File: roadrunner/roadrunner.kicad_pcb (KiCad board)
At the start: 2 copper layers, 216.9 x 86.9 mm, 52 parts, among them J1 Battery_conn, J2 battery_conn_r, SW1 SW_Push, SW10 SW_Push, SW10_r1 SW_Push, SW11 SW_Push, SW11_r1 SW_Push, SW12 SW_Push, SW12_r1 SW_Push, SW13 SW_Push, SW13_r1 SW_Push, SW14 SW_Push, SW14_r1 SW_Push, SW15 SW_Push, SW15_r1 SW_Push, SW16 SW_Push, SW16_r1 SW_Push, SW17 SW_Push, SW17_r1 SW_Push, SW1_r1 SW_Push, SW2 SW_Push, SW2_r1 SW_Push, SW3 SW_Push, SW3_r1 SW_Push, SW4 SW_Push, SW4_r1 SW_Push, SW5 SW_Push, SW5_r1 SW_Push, SW6 SW_Push, SW6_r1 SW_Push, SW7 SW_Push, SW7_r1 SW_Push, SW8 SW_Push, SW8_r1 SW_Push, SW9 SW_Push, SW9_r1 SW_Push, U1 ProMicro-kbd, U2 ProMicro-kbd

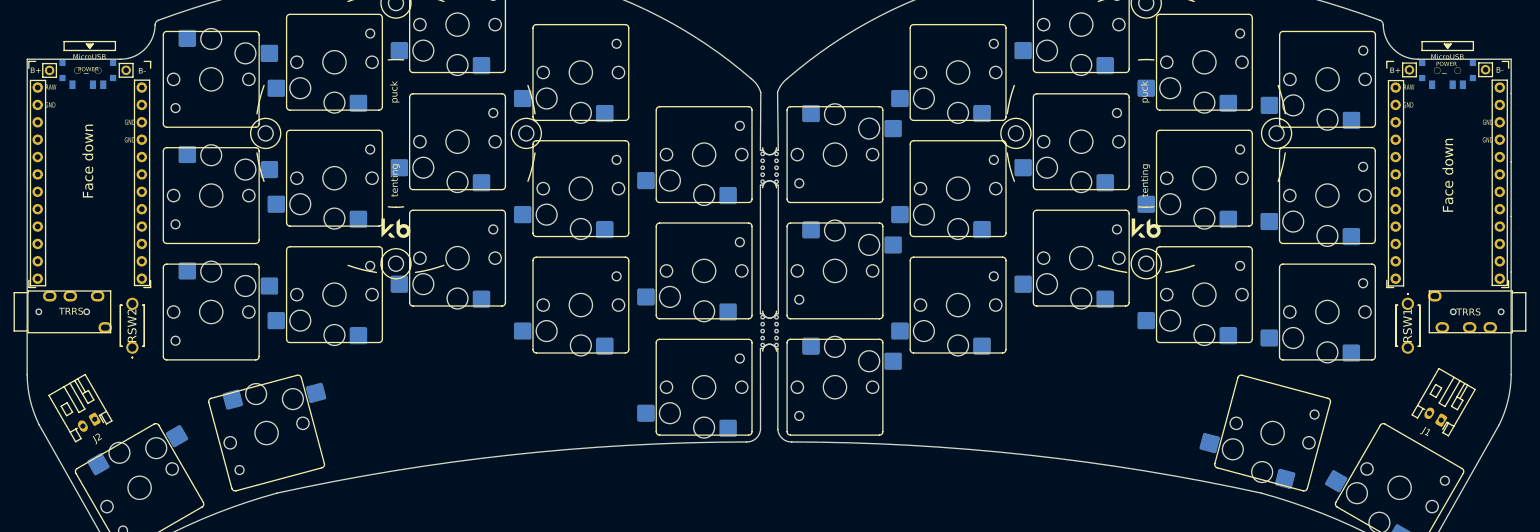
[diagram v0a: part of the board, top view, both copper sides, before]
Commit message: update schematic
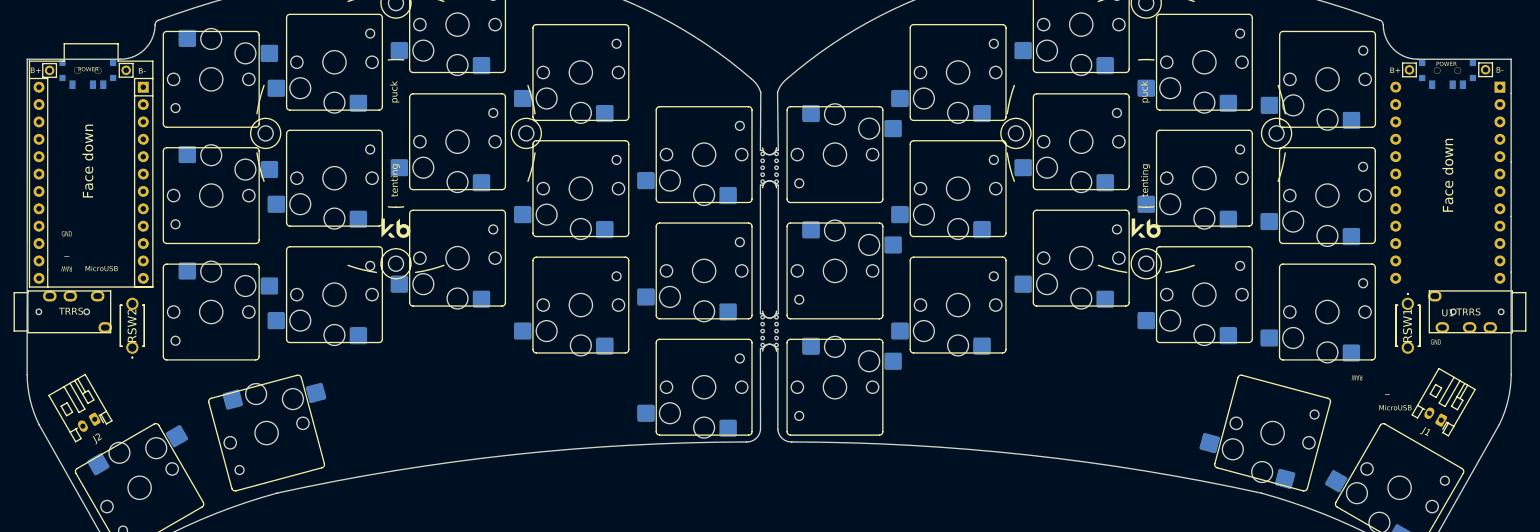
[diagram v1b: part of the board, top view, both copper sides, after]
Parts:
- U1, U2: footprint promicro:ProMicro_v3_min -> Arduino:Sparkfun_Pro_Micro; moved to B.Cu
- moved U2 16.8 mm to (43.8, 79.6)
- moved U1 15.4 mm to (243.1, 78.4)
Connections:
- U1 pad 1: (no net) -> Switch10
- U1 pad 10: (no net) -> Switch1
- U1 pad 11: (no net) -> Switch16
- U1 pad 12: (no net) -> Switch17
- U1 pad 13: (no net) -> Switch9
- U1 pad 14: (no net) -> Switch8
- U1 pad 15: (no net) -> Switch7
- U1 pad 16: (no net) -> Switch6
- U1 pad 17: (no net) -> Switch2
- U1 pad 18: (no net) -> Switch3
- U1 pad 19: (no net) -> Switch4
- U1 pad 2: (no net) -> Switch18
- U1 pad 20: (no net) -> Switch5
- U1 pad 21: (no net) -> vcc
- U1 pad 22: (no net) -> reset
- U1 pad 23: (no net) -> gnd
- U1 pad 24: (no net) -> raw
- U1 pad 3: (no net) -> gnd
- U1 pad 4: (no net) -> gnd
- U1 pad 5: (no net) -> Switch11
- U1 pad 6: (no net) -> Switch12
- U1 pad 7: (no net) -> Switch13
- U1 pad 8: (no net) -> Switch14
- U1 pad 9: (no net) -> Switch15
- U2 pad 1: (no net) -> Switch10_r
- U2 pad 10: (no net) -> Switch1_r
- U2 pad 11: (no net) -> Switch16_r
- U2 pad 12: (no net) -> Switch17_r
- U2 pad 13: (no net) -> Switch9_r
- U2 pad 14: (no net) -> Switch8_r
- U2 pad 15: (no net) -> Switch7_r
- U2 pad 16: (no net) -> Switch6_r
- U2 pad 17: (no net) -> Switch2_r
- U2 pad 18: (no net) -> Switch3_r
- U2 pad 19: (no net) -> Switch4_r
- U2 pad 2: (no net) -> Switch18_r
- U2 pad 20: (no net) -> Switch5_r
- U2 pad 21: (no net) -> vcc_r
- U2 pad 22: (no net) -> reset_r
- U2 pad 23: (no net) -> gnd_r
- U2 pad 24: (no net) -> raw_r
- U2 pad 3: (no net) -> gnd_r
- U2 pad 4: (no net) -> gnd_r
- U2 pad 5: (no net) -> Switch11_r
- U2 pad 6: (no net) -> Switch12_r
- U2 pad 7: (no net) -> Switch13_r
- U2 pad 8: (no net) -> Switch14_r
- U2 pad 9: (no net) -> Switch15_r

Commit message: update shape
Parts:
- TRRS1, TRRS2: footprint trrs:TRRS-PJ-320A -> Connector_Audio:Jack_3.5mm_PJ320E_Horizontal
- moved TRRS2 10.6 mm to (52.6, 88.2)
- moved TRRS1 9.47 mm to (250.7, 82.1)
- moved J2 1.77 mm to (54.3, 98.0)
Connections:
- TRRS1 pad R1: (no net) -> Switch18
- TRRS1 pad R2: (no net) -> vcc
- TRRS1 pad S: (no net) -> gnd
- TRRS1 pad T: (no net) -> gnd
- TRRS2 pad R1: (no net) -> Switch18_r
- TRRS2 pad R2: (no net) -> vcc_r
- TRRS2 pad S: (no net) -> gnd_r
- TRRS2 pad T: (no net) -> gnd_r
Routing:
- net gnd: track 0.00 -> 338.8 mm
- net gnd_r: track 0.00 -> 334.2 mm
- net Switch11_r: track 0.00 -> 108.4 mm
- net Switch6_r: track 0.00 -> 107.4 mm, vias 0 -> 1
- net Switch11: track 0.00 -> 104.3 mm, vias 0 -> 1
- net Switch4: track 0.00 -> 102.8 mm
- net Switch1_r: track 0.00 -> 89.4 mm, vias 0 -> 1
- net Switch2_r: track 0.00 -> 88.8 mm, vias 0 -> 1
- net Switch7: track 0.00 -> 88.7 mm, vias 0 -> 1
- net Switch1: track 0.00 -> 87.4 mm, vias 0 -> 1
- net Switch8_r: track 0.00 -> 86.5 mm, vias 0 -> 1
- net Switch7_r: track 0.00 -> 84.7 mm, vias 0 -> 1
- net Switch13: track 0.00 -> 80.2 mm, vias 0 -> 1
- net Switch12_r: track 0.00 -> 77.9 mm
- net Switch3_r: track 0.00 -> 77.6 mm
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- added copper zone on B.Cu, net gnd
- added copper zone on F.Cu, net gnd
- added copper zone on B.Cu, net gnd_r
- added copper zone on F.Cu, net gnd_r
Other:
- board size 216.9 x 86.9 mm -> 217.1 x 92.2 mm

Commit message: prepare board for order
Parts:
- added ? (x2): , , B.Cu at (225.2, 39.3)
- added ?: , , B.Cu at (174.2, 95.3)
- added ?: , , B.Cu at (254.2, 102.3)
- added ?: , , B.Cu at (186.2, 38.3)
- added ?: , , B.Cu at (212.2, 92.3)
- added REF**: MountingHole_3.2mm_M3, MountingHole:MountingHole_3.2mm_M3, F.Cu at (77.2, 39.3)
- added REF**: MountingHole_3.2mm_M3, MountingHole:MountingHole_3.2mm_M3, B.Cu at (167.2, 50.3)
- added REF**: MountingHole_3.2mm_M3, MountingHole:MountingHole_3.2mm_M3, B.Cu at (174.2, 95.3)
- added REF**: MountingHole_3.2mm_M3, MountingHole:MountingHole_3.2mm_M3, B.Cu at (186.2, 38.3)
- added REF**: MountingHole_3.2mm_M3, MountingHole:MountingHole_3.2mm_M3, F.Cu at (128.2, 95.3)
- added REF**: MountingHole_3.2mm_M3, MountingHole:MountingHole_3.2mm_M3, F.Cu at (116.2, 38.3)
- added REF**: MountingHole_3.2mm_M3, MountingHole:MountingHole_3.2mm_M3, F.Cu at (135.2, 50.3)
- added REF**: MountingHole_3.2mm_M3, MountingHole:MountingHole_3.2mm_M3, F.Cu at (48.2, 102.3)
- added REF**: MountingHole_3.2mm_M3, MountingHole:MountingHole_3.2mm_M3, F.Cu at (90.2, 92.3)
- added REF**: MountingHole_3.2mm_M3, MountingHole:MountingHole_3.2mm_M3, B.Cu at (212.2, 92.3)
- added REF**: MountingHole_3.2mm_M3, MountingHole:MountingHole_3.2mm_M3, B.Cu at (225.2, 39.3)
- added REF**: MountingHole_3.2mm_M3, MountingHole:MountingHole_3.2mm_M3, B.Cu at (254.2, 102.3)
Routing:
- net gnd: track 338.8 -> 4.99 mm
- net gnd_r: track 334.2 -> 1.03 mm
- net Switch4: track 102.8 -> 116.7 mm
- net Switch11: track 104.3 -> 113.1 mm
- net Switch13_r: track 56.0 -> 63.6 mm
- net Switch12_r: track 77.9 -> 84.0 mm
- net Switch8_r: track 86.5 -> 92.5 mm
- net Switch6_r: track 107.4 -> 112.6 mm
- net Switch9: track 64.7 -> 69.8 mm
- net Switch11_r: track 108.4 -> 112.7 mm
- net Switch1_r: track 89.4 -> 93.2 mm
- net Switch3: track 44.2 -> 47.7 mm
- net Switch6: track 66.5 -> 69.6 mm
- net Switch18_r: track 40.0 -> 42.6 mm
- net Switch7_r: track 84.7 -> 87.2 mm
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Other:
- board text added: "BT+"
- board text added: "By N8"
- board text added: "Do not solder board to this side"
- board text added: "RoadRunner v1.0.0"

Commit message: basic v2 designs
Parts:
- removed ? (x6): , 
- removed REF** (x12): MountingHole_3.2mm_M3, MountingHole:MountingHole_3.2mm_M3
- removed TRRS1, TRRS2: AudioJack4, Connector_Audio:Jack_3.5mm_PJ320E_Horizontal
- removed mouse-bite-2mm-slot1, mouse-bite-2mm-slot2: VAL**, Duckyb-Parts:mouse-bite-5mm-slot-with-space-for-track
- added G***: LOGO, LOGO, F.Cu at (79.3, 152.9)
- added G***: LOGO, LOGO, B.Cu at (155.6, 153.7)
- added G***: LOGO, LOGO, B.Cu at (117.0, 138.2)
- moved U2 11.6 mm to (32.4, 81.7)
- moved Bat+r1 11.4 mm to (35.2, 50.2)
- moved SW_POWERR1 11.4 mm to (40.8, 50.2)
- moved BatGNDr1 11.4 mm to (46.4, 50.2)
- moved RSW2 10.7 mm to (48.6, 84.2), turned to -90 degrees
- moved U1 9.70 mm to (252.5, 80.6)
- moved RSW1 9.54 mm to (254.1, 84.4)
- moved BatGND1 9.54 mm to (265.5, 50.1)
- moved J1 9.54 mm to (259.0, 101.4)
- moved SW_POWER1 9.54 mm to (259.9, 50.3)
- moved Bat+1 9.54 mm to (254.4, 50.2)
- moved J2 8.53 mm to (45.8, 98.4)
- moved SW11_r1 8.22 mm to (133.8, 94.3)
- moved SW13_r1 8.22 mm to (97.7, 75.5)
- moved SW14_r1 8.22 mm to (79.7, 80.8)
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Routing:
- net Switch4: track 116.7 -> 0.00 mm
- net Switch11: track 113.1 -> 0.00 mm
- net Switch11_r: track 112.7 -> 0.00 mm
- net Switch6_r: track 112.6 -> 0.00 mm
- net Switch1_r: track 93.2 -> 0.00 mm
- net Switch8_r: track 92.5 -> 0.00 mm
- net Switch7: track 89.7 -> 0.00 mm
- net Switch2_r: track 89.0 -> 0.00 mm
- net Switch1: track 87.7 -> 0.00 mm
- net Switch7_r: track 87.2 -> 0.00 mm
- net Switch12_r: track 84.0 -> 0.00 mm
- net Switch13: track 81.7 -> 0.00 mm
- net Switch3_r: track 79.9 -> 0.00 mm
- net Switch10: track 71.6 -> 0.00 mm
- net Switch9: track 69.8 -> 0.00 mm
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- removed copper zone on B.Cu, net gnd
- removed copper zone on F.Cu, net gnd
- removed copper zone on B.Cu, net gnd_r
- removed copper zone on F.Cu, net gnd_r
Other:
- board size 217.1 x 92.2 mm -> 252.3 x 97.3 mm
- board text added: "RoadRunner v2.0.0"
- board text removed: "RoadRunner v1.0.0"

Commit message: move button
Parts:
- moved RSW1 1.71 mm to (252.4, 84.2)
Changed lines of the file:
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@@
   )
   (footprint "reset_switch:PTS636SP43LFS" (layer "F.Cu")
-    (at 254.1348 84.3547 -90)
+    (at 252.43 84.23 -90)
     (descr "PTS636 SP43 LFS-1")
     (tags "Switch")

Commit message: begin adding diodes
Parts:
- removed G*** (x3): LOGO, LOGO
- added D1: 1N4148W, Diode_SMD:D_SOD-123, B.Cu at (170.9, 60.0)
- added D10: 1N4148W, Diode_SMD:D_SOD-123, B.Cu at (226.3, 75.4)
- added D11: 1N4148W, Diode_SMD:D_SOD-123, B.Cu at (171.4, 96.3)
- added D12: 1N4148W, Diode_SMD:D_SOD-123, B.Cu at (172.6, 82.5)
- added D13: 1N4148W, Diode_SMD:D_SOD-123, B.Cu at (190.4, 83.0)
- added D14: 1N4148W, Diode_SMD:D_SOD-123, B.Cu at (208.4, 88.7)
- added D15: 1N4148W, Diode_SMD:D_SOD-123, B.Cu at (226.4, 83.1)
- added D16: 1N4148W, Diode_SMD:D_SOD-123, B.Cu at (218.1, 95.6)
- added D17: 1N4148W, Diode_SMD:D_SOD-123, B.Cu at (237.9, 101.2)
- added D18: 1N4148W, Diode_SMD:D_SOD-123, B.Cu at (70.5, 41.4)
- added D19: 1N4148W, Diode_SMD:D_SOD-123, B.Cu at (74.5, 55.4)
- added D2: 1N4148W, Diode_SMD:D_SOD-123, B.Cu at (171.9, 47.1)
- added D20: 1N4148W, Diode_SMD:D_SOD-123, B.Cu at (79.9, 134.0)
- added D21: 1N4148W, Diode_SMD:D_SOD-123, B.Cu at (91.5, 142.4)
- added D22: 1N4148W, Diode_SMD:D_SOD-123, B.Cu at (92.4, 135.6)
- added D23: 1N4148W, Diode_SMD:D_SOD-123, B.Cu at (95.1, 127.3)
- added D24: 1N4148W, Diode_SMD:D_SOD-123, B.Cu at (84.7, 138.2)
- added D25: 1N4148W, Diode_SMD:D_SOD-123, B.Cu at (85.9, 131.5)
- added D26: 1N4148W, Diode_SMD:D_SOD-123, B.Cu at (103.7, 147.0)
- added D27: 1N4148W, Diode_SMD:D_SOD-123, B.Cu at (84.3, 144.2)
- added D28: 1N4148W, Diode_SMD:D_SOD-123, B.Cu at (98.0, 157.9)
- added D29: 1N4148W, Diode_SMD:D_SOD-123, B.Cu at (78.5, 139.6)
- added D3: 1N4148W, Diode_SMD:D_SOD-123, B.Cu at (189.9, 41.1)
- added D30: 1N4148W, Diode_SMD:D_SOD-123, B.Cu at (90.3, 150.2)
- added D31: 1N4148W, Diode_SMD:D_SOD-123, B.Cu at (96.7, 149.6)
- added D32: 1N4148W, Diode_SMD:D_SOD-123, B.Cu at (101.7, 135.9)
- added D33: 1N4148W, Diode_SMD:D_SOD-123, B.Cu at (88.1, 123.6)
- added D34: 1N4148W, Diode_SMD:D_SOD-123, B.Cu at (80.7, 147.1)
- added D4: 1N4148W, Diode_SMD:D_SOD-123, B.Cu at (208.0, 46.3)
- added D5: 1N4148W, Diode_SMD:D_SOD-123, B.Cu at (225.9, 49.0)
- added D6: 1N4148W, Diode_SMD:D_SOD-123, B.Cu at (170.9, 77.1)
- added D7: 1N4148W, Diode_SMD:D_SOD-123, B.Cu at (172.3, 65.6)
- added D8: 1N4148W, Diode_SMD:D_SOD-123, B.Cu at (190.2, 66.3)
- added D9: 1N4148W, Diode_SMD:D_SOD-123, B.Cu at (208.1, 63.6)
- added J4: niceview_left, Connector_PinHeader_2.54mm:PinHeader_1x05_P2.54mm_Vertical, F.Cu at (260.1, 84.5)
- added J5: niceview_right, Connector_PinHeader_2.54mm:PinHeader_1x05_P2.54mm_Vertical, F.Cu at (35.8, 83.8)
- added mouse-bite-2mm-slot1: VAL**, Duckyb-Parts:mouse-bite-5mm-slot-with-space-for-track, F.Cu at (148.2, 52.2)
- added mouse-bite-2mm-slot1: VAL**, Duckyb-Parts:mouse-bite-5mm-slot-with-space-for-track, F.Cu at (148.2, 79.5)
- moved RSW1 7.24 mm to (246.4, 88.3)
- moved SW1 5.45 mm to (162.6, 60.3)
- moved SW11 5.45 mm to (162.6, 94.3)
- moved SW12 5.45 mm to (180.6, 82.3)
- moved SW13 5.45 mm to (198.6, 75.4)
- moved SW14 5.45 mm to (216.6, 80.7)
- moved SW17 5.45 mm to (245.2, 109.0)
- moved SW2 5.45 mm to (180.6, 48.3)
- moved SW3 5.45 mm to (198.6, 41.3)
- moved SW4 5.45 mm to (216.6, 46.8)
- moved SW5 5.45 mm to (234.6, 49.3)
- moved SW6 5.45 mm to (162.6, 77.3)
- moved SW7 5.45 mm to (180.6, 65.2)
- moved SW8 5.45 mm to (198.6, 58.4)
- moved SW9 5.45 mm to (216.6, 63.7)
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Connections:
- SW1 pad 1: Switch11 -> unconnected-(SW1-Pad1)
- SW1 pad 2: gnd -> Net-(SW1-Pad2)
- SW10 pad 1: Switch14 -> COL4
- SW10 pad 2: gnd -> Net-(SW10-Pad2)
- SW10_r1 pad 1: Switch10_r -> COL0_r
- SW10_r1 pad 2: gnd_r -> Net-(SW10_r1-Pad2)
- SW11 pad 1: Switch4 -> COL0
- SW11 pad 2: gnd -> Net-(SW11-Pad2)
- SW11_r1 pad 1: Switch11_r -> COL4_r
- SW11_r1 pad 2: gnd_r -> Net-(SW11_r1-Pad2)
- SW12 pad 1: Switch9 -> COL1
- SW12 pad 2: gnd -> Net-(SW12-Pad2)
- SW12_r1 pad 1: Switch12_r -> COL3_r
- SW12_r1 pad 2: gnd_r -> Net-(SW12_r1-Pad2)
- SW13 pad 1: Switch16 -> COL2
- SW13 pad 2: gnd -> Net-(SW13-Pad2)
- SW13_r1 pad 1: Switch13_r -> COL2_r
- SW13_r1 pad 2: gnd_r -> Net-(SW13_r1-Pad2)
- SW14 pad 1: Switch17 -> COL3
- SW14 pad 2: gnd -> Net-(SW14-Pad2)
- SW14_r1 pad 1: Switch14_r -> COL1_r
- SW14_r1 pad 2: gnd_r -> Net-(SW14_r1-Pad2)
- SW15 pad 1: Switch15 -> COL4
- SW15 pad 2: gnd -> Net-(SW15-Pad2)
- SW15_r1 pad 1: Switch15_r -> COL0_r
- SW15_r1 pad 2: gnd_r -> Net-(SW15_r1-Pad2)
- SW16 pad 1: Switch5 -> COL3
- SW16 pad 2: gnd -> Net-(SW16-Pad2)
- SW16_r1 pad 1: Switch16_r -> COL1_r
- SW16_r1 pad 2: gnd_r -> Net-(SW16_r1-Pad2)
- SW17 pad 1: Switch10 -> COL4
- SW17 pad 2: gnd -> Net-(SW17-Pad2)
- SW17_r1 pad 1: Switch17_r -> COL0_r
- SW17_r1 pad 2: gnd_r -> Net-(SW17_r1-Pad2)
- SW1_r1 pad 1: Switch1_r -> unconnected-(SW1_r1-Pad1)
- SW1_r1 pad 2: gnd_r -> Net-(SW1_r1-Pad2)
- SW2 pad 1: Switch1 -> COL1
- SW2 pad 2: gnd -> Net-(SW2-Pad2)
- SW2_r1 pad 1: Switch2_r -> unconnected-(SW2_r1-Pad1)
- SW2_r1 pad 2: gnd_r -> Net-(SW2_r1-Pad2)
- SW3 pad 1: Switch6 -> COL2
- SW3 pad 2: gnd -> Net-(SW3-Pad2)
- SW3_r1 pad 1: Switch3_r -> unconnected-(SW3_r1-Pad1)
- SW3_r1 pad 2: gnd_r -> Net-(SW3_r1-Pad2)
- SW4 pad 1: Switch12 -> COL3
- SW4 pad 2: gnd -> Net-(SW4-Pad2)
- SW4_r1 pad 1: Switch4_r -> COL1_r
- SW4_r1 pad 2: gnd_r -> Net-(SW4_r1-Pad2)
- SW5 pad 1: Switch2 -> COL4
- SW5 pad 2: gnd -> Net-(SW5-Pad2)
- SW5_r1 pad 1: Switch5_r -> COL0_r
- SW5_r1 pad 2: gnd_r -> Net-(SW5_r1-Pad2)
- SW6 pad 1: Switch7 -> COL0
- SW6 pad 2: gnd -> Net-(SW6-Pad2)
- SW6_r1 pad 1: Switch6_r -> COL4_r
- SW6_r1 pad 2: gnd_r -> Net-(SW6_r1-Pad2)
- SW7 pad 1: Switch13 -> COL1
- SW7 pad 2: gnd -> Net-(SW7-Pad2)
- SW7_r1 pad 1: Switch7_r -> COL3_r
- SW7_r1 pad 2: gnd_r -> Net-(SW7_r1-Pad2)
- SW8 pad 1: Switch3 -> COL2
- SW8 pad 2: gnd -> Net-(SW8-Pad2)
- SW8_r1 pad 1: Switch8_r -> COL2_r
- SW8_r1 pad 2: gnd_r -> Net-(SW8_r1-Pad2)
- SW9 pad 1: Switch8 -> COL3
- SW9 pad 2: gnd -> Net-(SW9-Pad2)
- SW9_r1 pad 1: Switch9_r -> COL1_r
- SW9_r1 pad 2: gnd_r -> Net-(SW9_r1-Pad2)
- U1 pad 1: Switch10 -> CS
- U1 pad 10: Switch1 -> ROW1
- U1 pad 11: Switch16 -> ROW2
- U1 pad 12: Switch17 -> ROW3
- U1 pad 13: Switch9 -> COL1
- U1 pad 14: Switch8 -> COL0
- U1 pad 15: Switch7 -> COL2
- U1 pad 16: Switch6 -> COL3
- U1 pad 17: Switch2 -> COL4
- U1 pad 18: Switch3 -> unconnected-(U1-Pad18)
- U1 pad 19: Switch4 -> unconnected-(U1-Pad19)
- U1 pad 2: Switch18 -> unconnected-(U1-Pad2)
- U1 pad 20: Switch5 -> unconnected-(U1-Pad20)
- U1 pad 5: Switch11 -> MOSI
- U1 pad 6: Switch12 -> SCK
- U1 pad 7: Switch13 -> unconnected-(U1-Pad7)
- U1 pad 8: Switch14 -> unconnected-(U1-Pad8)
- U1 pad 9: Switch15 -> ROW0
- U2 pad 1: Switch10_r -> CS_R
- U2 pad 10: Switch1_r -> ROW1_r
- U2 pad 11: Switch16_r -> ROW2_r
- U2 pad 12: Switch17_r -> ROW3_r
- U2 pad 13: Switch9_r -> COL1_r
- U2 pad 14: Switch8_r -> COL0_r
- U2 pad 15: Switch7_r -> COL2_r
- U2 pad 16: Switch6_r -> COL3_r
- U2 pad 17: Switch2_r -> COL4_r
- U2 pad 18: Switch3_r -> unconnected-(U2-Pad18)
- U2 pad 19: Switch4_r -> unconnected-(U2-Pad19)
- U2 pad 2: Switch18_r -> unconnected-(U2-Pad2)
- U2 pad 20: Switch5_r -> unconnected-(U2-Pad20)
- U2 pad 5: Switch11_r -> MOSI_r
- U2 pad 6: Switch12_r -> SCK_r
- U2 pad 7: Switch13_r -> unconnected-(U2-Pad7)
- U2 pad 8: Switch14_r -> unconnected-(U2-Pad8)
- U2 pad 9: Switch15_r -> ROW0_r
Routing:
- net Switch9_r: vias 2 -> 0
- net Switch8_r: vias 1 -> 0
- net Switch7_r: vias 1 -> 0
- net Switch7: vias 1 -> 0
- net Switch6_r: vias 1 -> 0
- net Switch6: vias 1 -> 0
- net Switch4_r: vias 1 -> 0
- net Switch3: vias 1 -> 0
- net Switch2_r: vias 1 -> 0
- net Switch1_r: vias 1 -> 0
- net Switch17: vias 1 -> 0
- net Switch16: vias 1 -> 0
- net Switch15: vias 1 -> 0
- net Switch14: vias 1 -> 0
- net Switch13: vias 1 -> 0
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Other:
- board size 252.3 x 97.3 mm -> 246.8 x 97.3 mm
- board text removed: "v1.0"
